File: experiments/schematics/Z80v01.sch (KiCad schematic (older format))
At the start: 0 parts

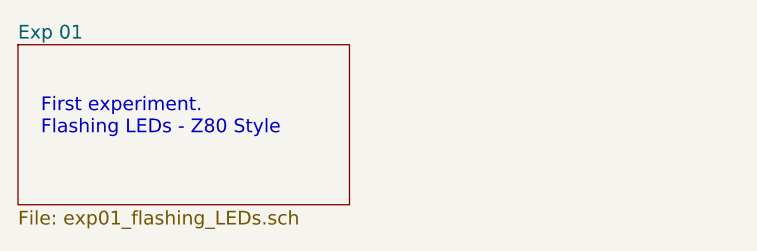
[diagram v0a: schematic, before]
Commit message: LED Debug board and defining the "bus" pinout
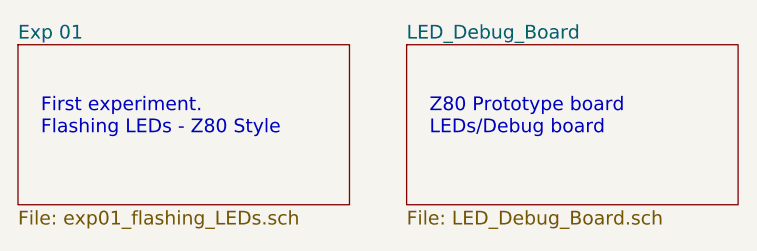
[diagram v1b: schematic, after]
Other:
- note added: "Z80 Prototype board\nLEDs/Debug board"
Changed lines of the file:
@@
 $Descr A4 11693 8268
 encoding utf-8
-Sheet 1 2
+Sheet 1 3
 Title ""
 Date ""
@@
 Text Notes 850  1150 0    60   ~ 0
 First experiment.\nFlashing LEDs - Z80 Style
+$Sheet
+S 2450 750  1450 700
+U 58B3FB39
+F0 "LED_Debug_Board" 60
+F1 "LED_Debug_Board.sch" 60
+$EndSheet
+Text Notes 2550 1150 0    60   ~ 0
+Z80 Prototype board\nLEDs/Debug board
 $EndSCHEMATC
